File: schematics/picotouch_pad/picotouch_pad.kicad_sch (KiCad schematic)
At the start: 82 parts, among them SW1 1, SW10 1, SW11 1, SW12 1, SW13 1, SW14 1, SW15 1, SW16 1, SW17 1, SW18 1, SW19 1, SW2 1, SW20 1, SW21 1, SW22 1, SW23 1, SW3 1, SW4 1, SW5 1, SW6 1, SW7 1, SW8 1, SW9 1, U1 Pico

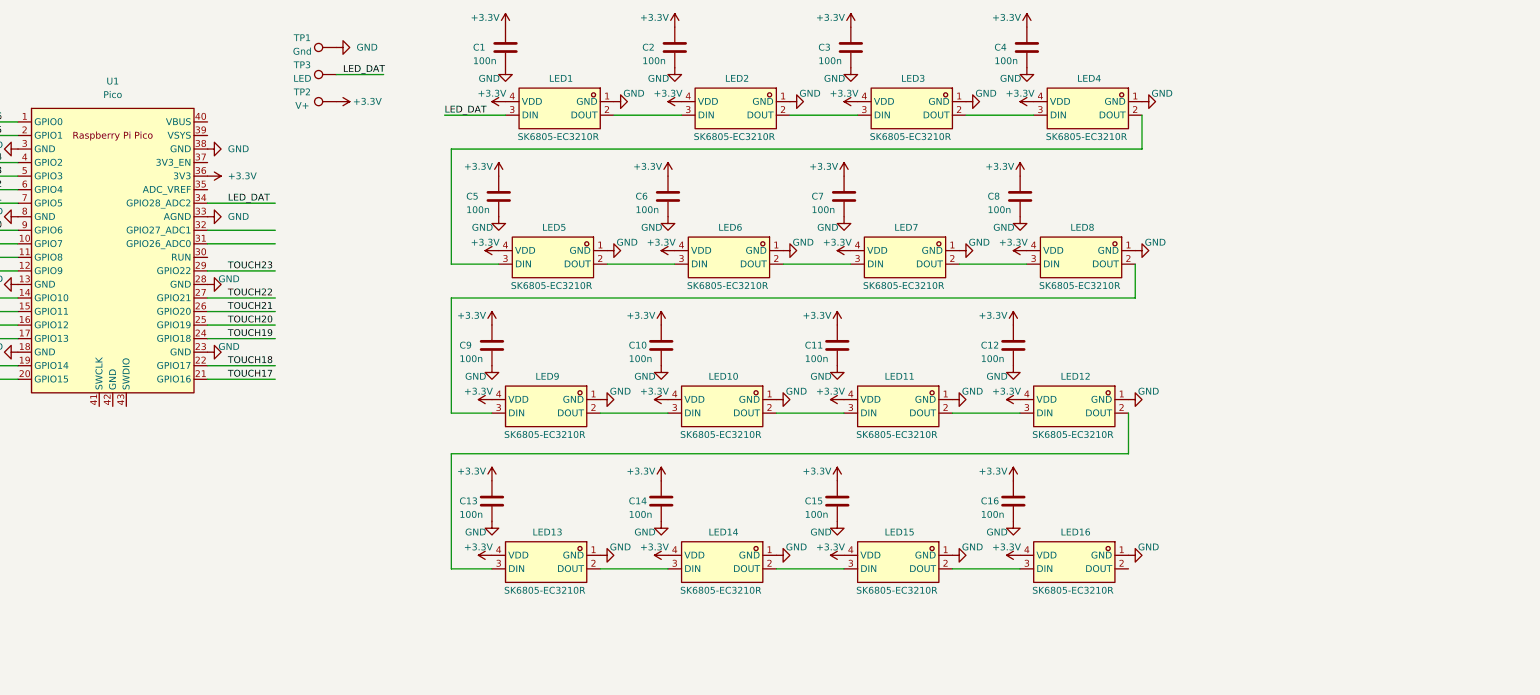
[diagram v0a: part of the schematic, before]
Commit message: new pcb with sk6812side
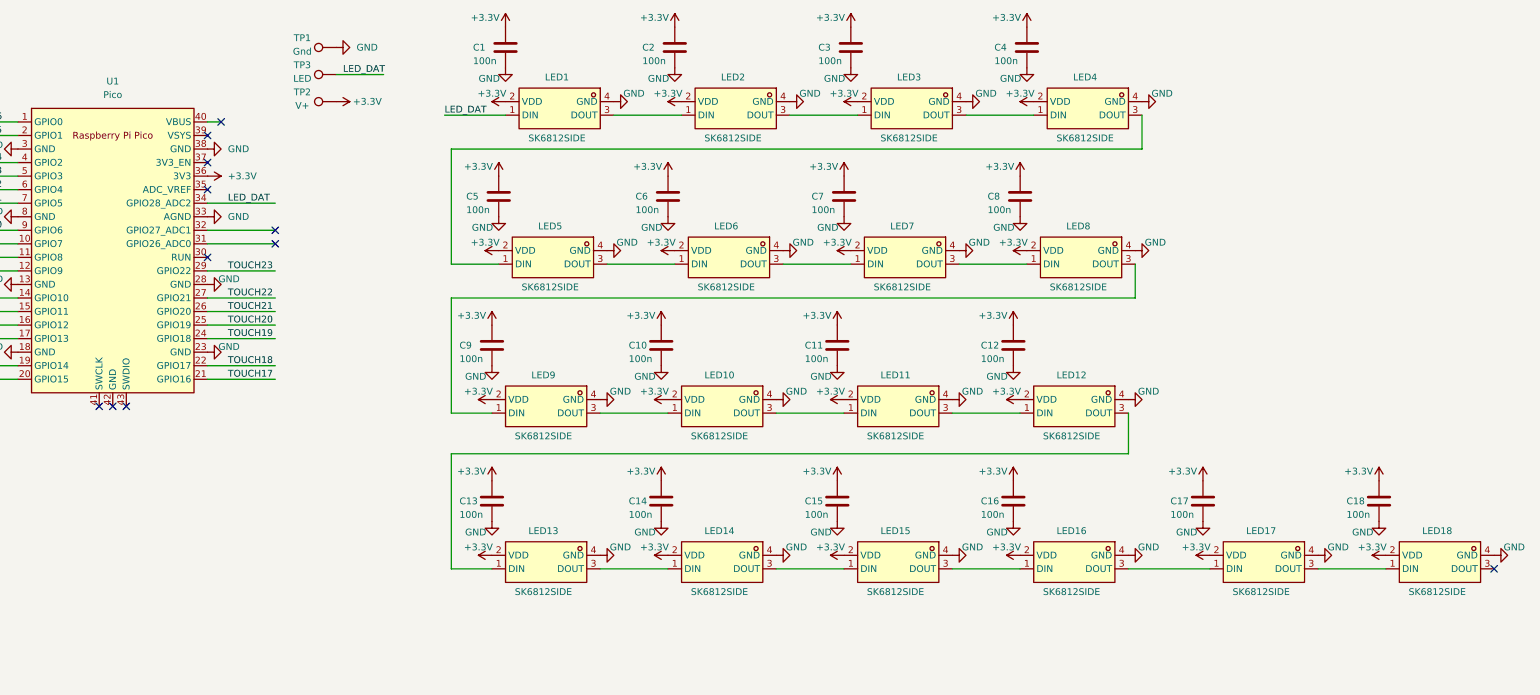
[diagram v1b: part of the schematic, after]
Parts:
- removed LED1, LED10, LED11, LED12, LED13, LED14, LED15, LED16, LED2, LED3, LED4, LED5, LED6, LED7, LED8, LED9: SK6805-EC3210R, todbot_stuff:LED-SMD_4P-L3.2-W1.5_SK6805-EC3210R-keepout, symbol todbot_stuff:SK6805-EC3210R
- added C17, C18: 100n, Capacitor_SMD:C_0603_1608Metric, symbol Device:C
- added LED1, LED10, LED11, LED12, LED13, LED14, LED15, LED16, LED17, LED18, LED2, LED3, LED4, LED5, LED6, LED7, LED8, LED9: SK6812SIDE, todbot_stuff:LED-SMD_4P-L4.0-W1.6-L-keepoutrev, symbol todbot_stuff:SK6812SIDE
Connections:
- net +3.3V: now also C17.1, C18.1, LED1.2 (VDD), LED10.2 (VDD), LED11.2 (VDD), LED12.2 (VDD), LED13.2 (VDD), LED14.2 (VDD), LED15.2 (VDD), LED16.2 (VDD), LED17.2 (VDD), LED18.2 (VDD), LED2.2 (VDD), LED3.2 (VDD), LED4.2 (VDD), LED5.2 (VDD), LED6.2 (VDD), LED7.2 (VDD), LED8.2 (VDD), LED9.2 (VDD)
- net GND: now also C17.2, C18.2, LED1.4 (GND), LED10.4 (GND), LED11.4 (GND), LED12.4 (GND), LED13.4 (GND), LED14.4 (GND), LED15.4 (GND), LED16.4 (GND), LED17.4 (GND), LED18.4 (GND), LED2.4 (GND), LED3.4 (GND), LED4.4 (GND), LED5.4 (GND), LED6.4 (GND), LED7.4 (GND), LED8.4 (GND), LED9.4 (GND)
- net LED_DAT: now also LED1.1 (DIN)
- new net: LED12.3 (DOUT), LED13.1 (DIN)
- new net: LED13.3 (DOUT), LED14.1 (DIN)
- new net: LED6.3 (DOUT), LED7.1 (DIN)
- new net: LED7.3 (DOUT), LED8.1 (DIN)
- new net: LED10.1 (DIN), LED9.3 (DOUT)
- new net: LED10.3 (DOUT), LED11.1 (DIN)
- new net: LED1.3 (DOUT), LED2.1 (DIN)
- new net: LED2.3 (DOUT), LED3.1 (DIN)
- new net: LED3.3 (DOUT), LED4.1 (DIN)
- new net: LED8.3 (DOUT), LED9.1 (DIN)
- new net: LED14.3 (DOUT), LED15.1 (DIN)
- new net: LED15.3 (DOUT), LED16.1 (DIN)
- new net: LED16.3 (DOUT), LED17.1 (DIN)
- new net: LED5.3 (DOUT), LED6.1 (DIN)
- new net: LED4.3 (DOUT), LED5.1 (DIN)
- new net: LED17.3 (DOUT), LED18.1 (DIN)
- new net: LED11.3 (DOUT), LED12.1 (DIN)
- no-connect marks 0 -> 11

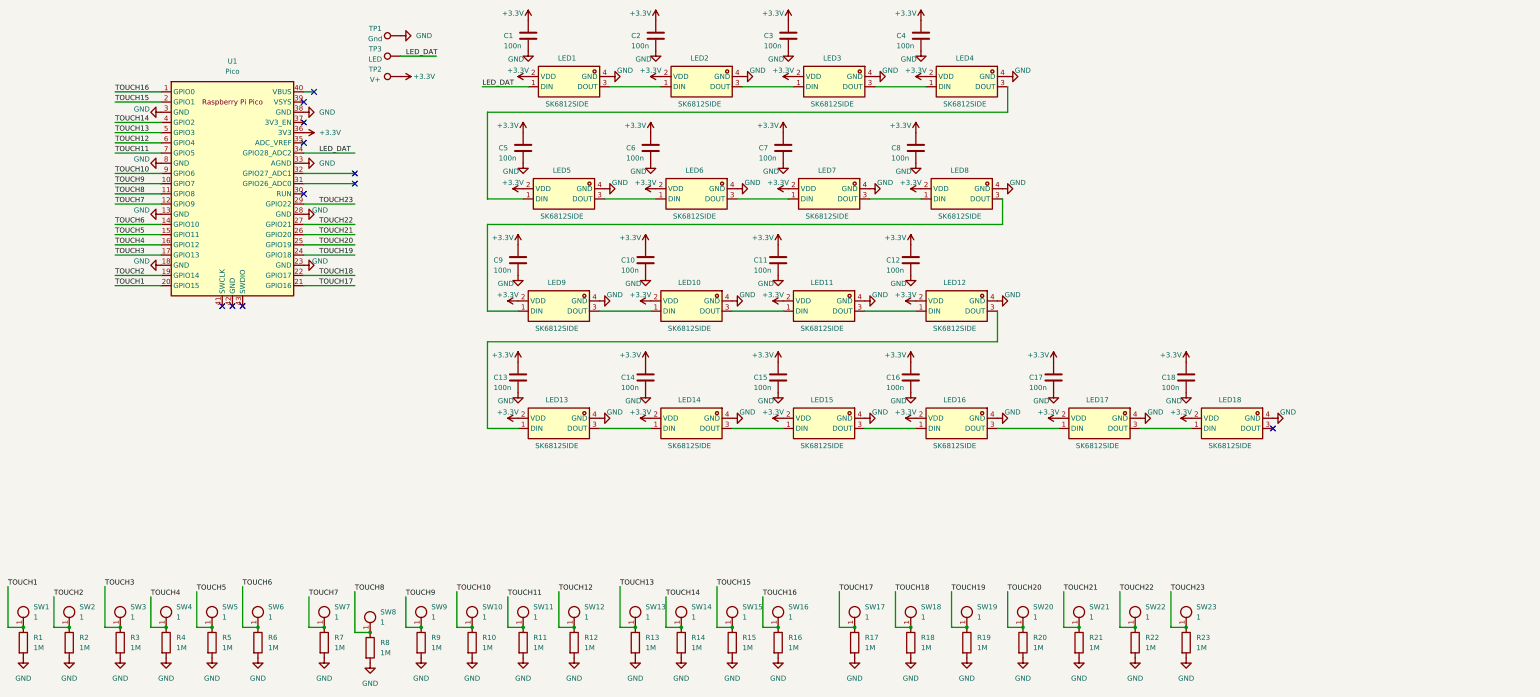
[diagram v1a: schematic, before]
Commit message: add battery circuit
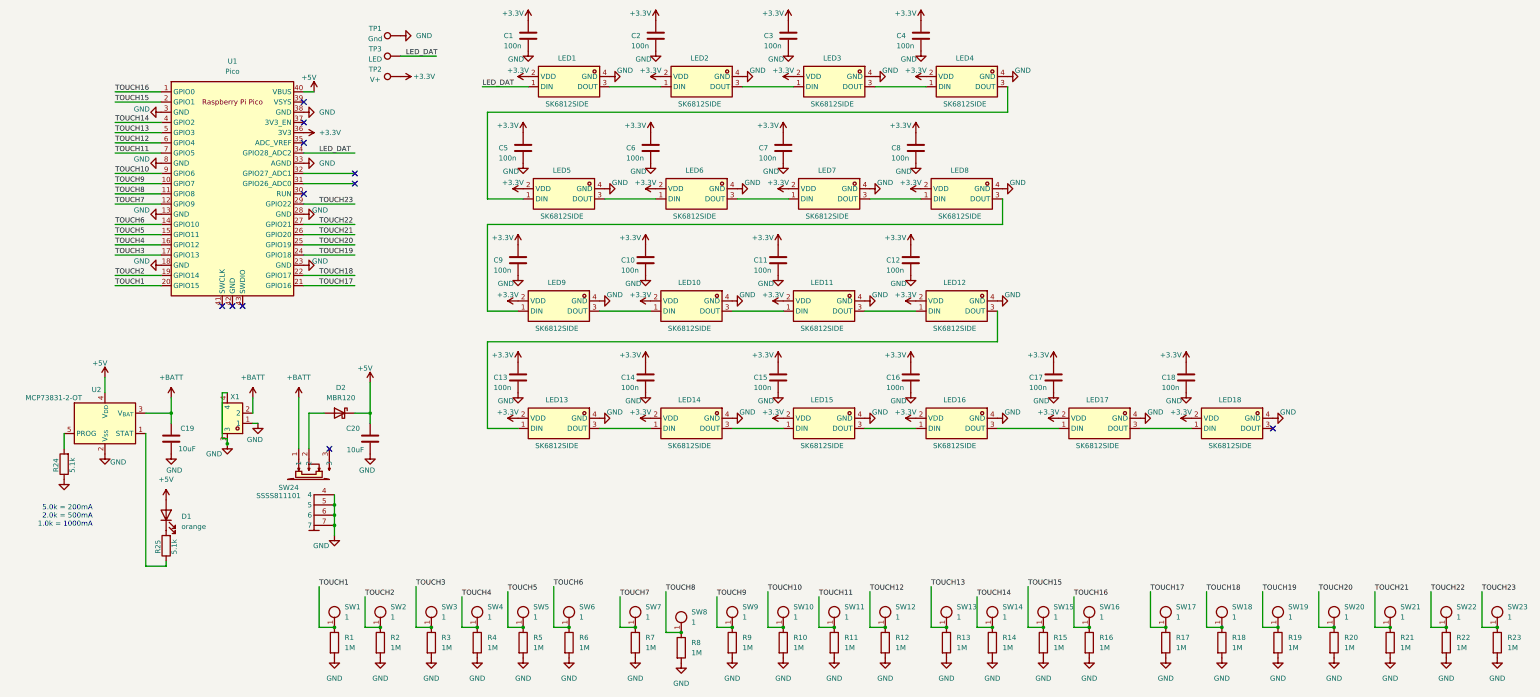
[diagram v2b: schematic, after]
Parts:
- added C19, C20: 10uF, Capacitor_SMD:C_0603_1608Metric, symbol Device:C
- added D1: orange, LED_SMD:LED_0603_1608Metric, symbol Device:LED
- added D2: MBR120, Diode_SMD:D_SOD-123F, symbol Device:D_Schottky
- added R24, R25: 5.1k, Resistor_SMD:R_0603_1608Metric, symbol Device:R
- added SW24: SSSS811101, easyeda2kicad:SW-SMD_SSSS811101, symbol easyeda2kicad:SSSS811101
- added U2: MCP73831-2-OT, Package_TO_SOT_SMD:SOT-23-5, symbol Battery_Management:MCP73831-2-OT
- added X1: AFC20-S02ACA-00, easyeda2kicad:CONN-SMD_AFC20-S02ACA-00, symbol easyeda2kicad:AFC20-S02ACA-00
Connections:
- net GND: now also C19.2, C20.2, R24.1, SW24.4, SW24.5, SW24.6, SW24.7, U2.2 (V_{SS}), X1.1, X1.3, X1.4
- net +5V: now reaches U1.40 (VBUS)
- net +5V: now also C20.1, D1.2 (A), D2.1 (K), U2.4 (V_{DD})
- new net: R25.1, U2.1 (STAT)
- new net: R24.2, U2.5 (PROG)
- new net: D1.1 (K), R25.2
- new net: D2.2 (A), SW24.2
- new net +BATT: C19.1, SW24.1, U2.3 (V_{BAT}), X1.2
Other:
- note added: "5.0k = 200mA 2.0k = 500mA 1.0k = 1000mA"
- moved on the sheet: R1, R10, R11, R12, R13, R14, R15, R16, R17, R18, R19, R2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

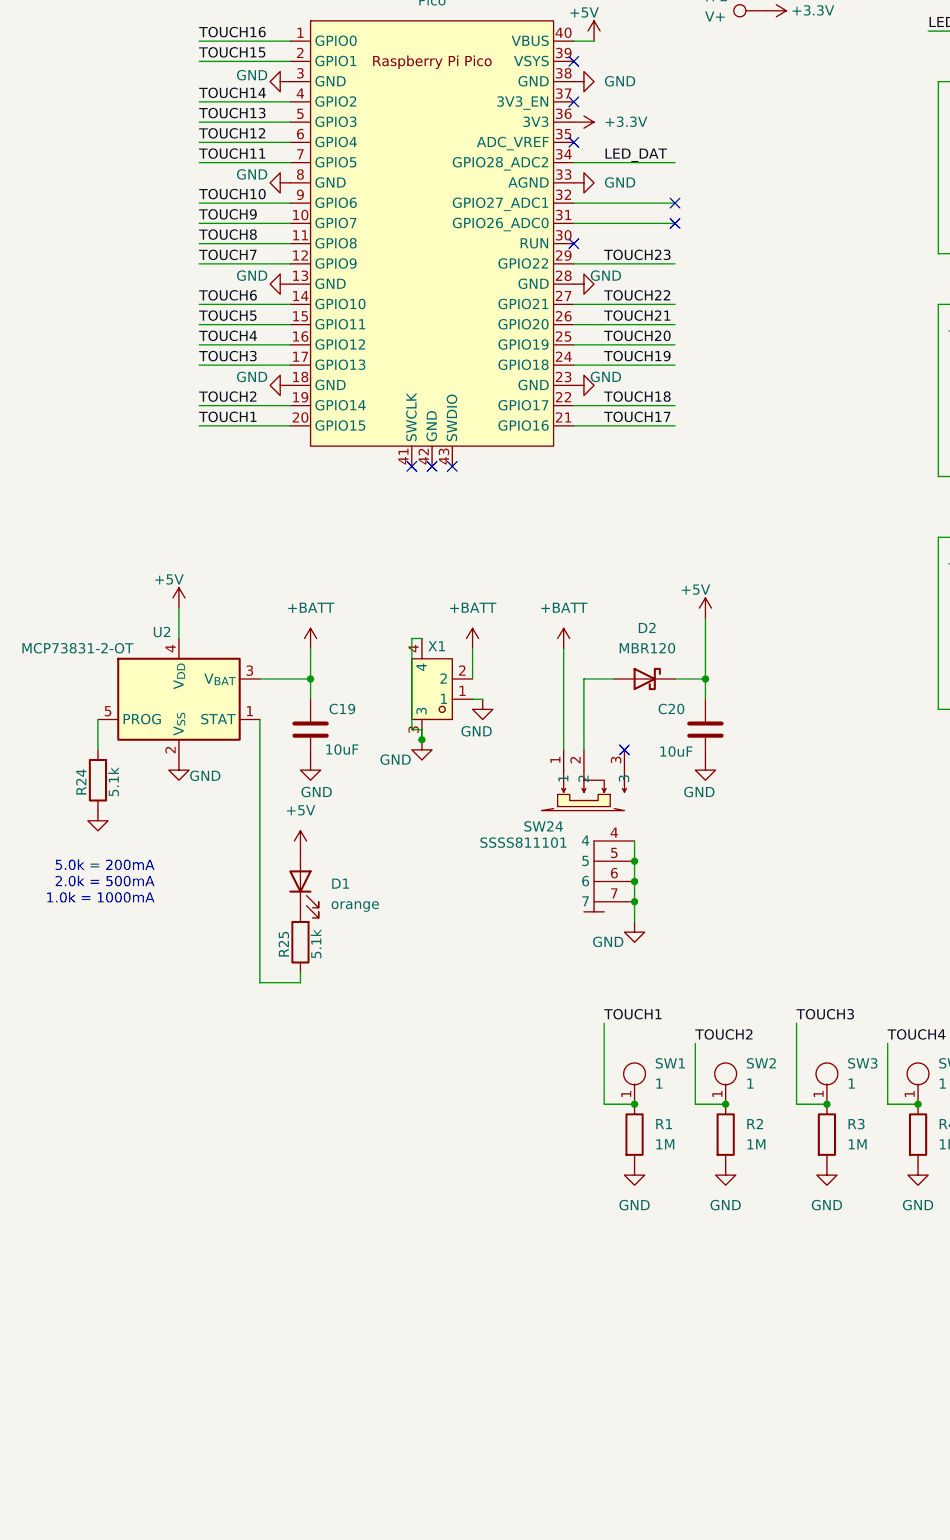
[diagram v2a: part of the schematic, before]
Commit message: add midi out
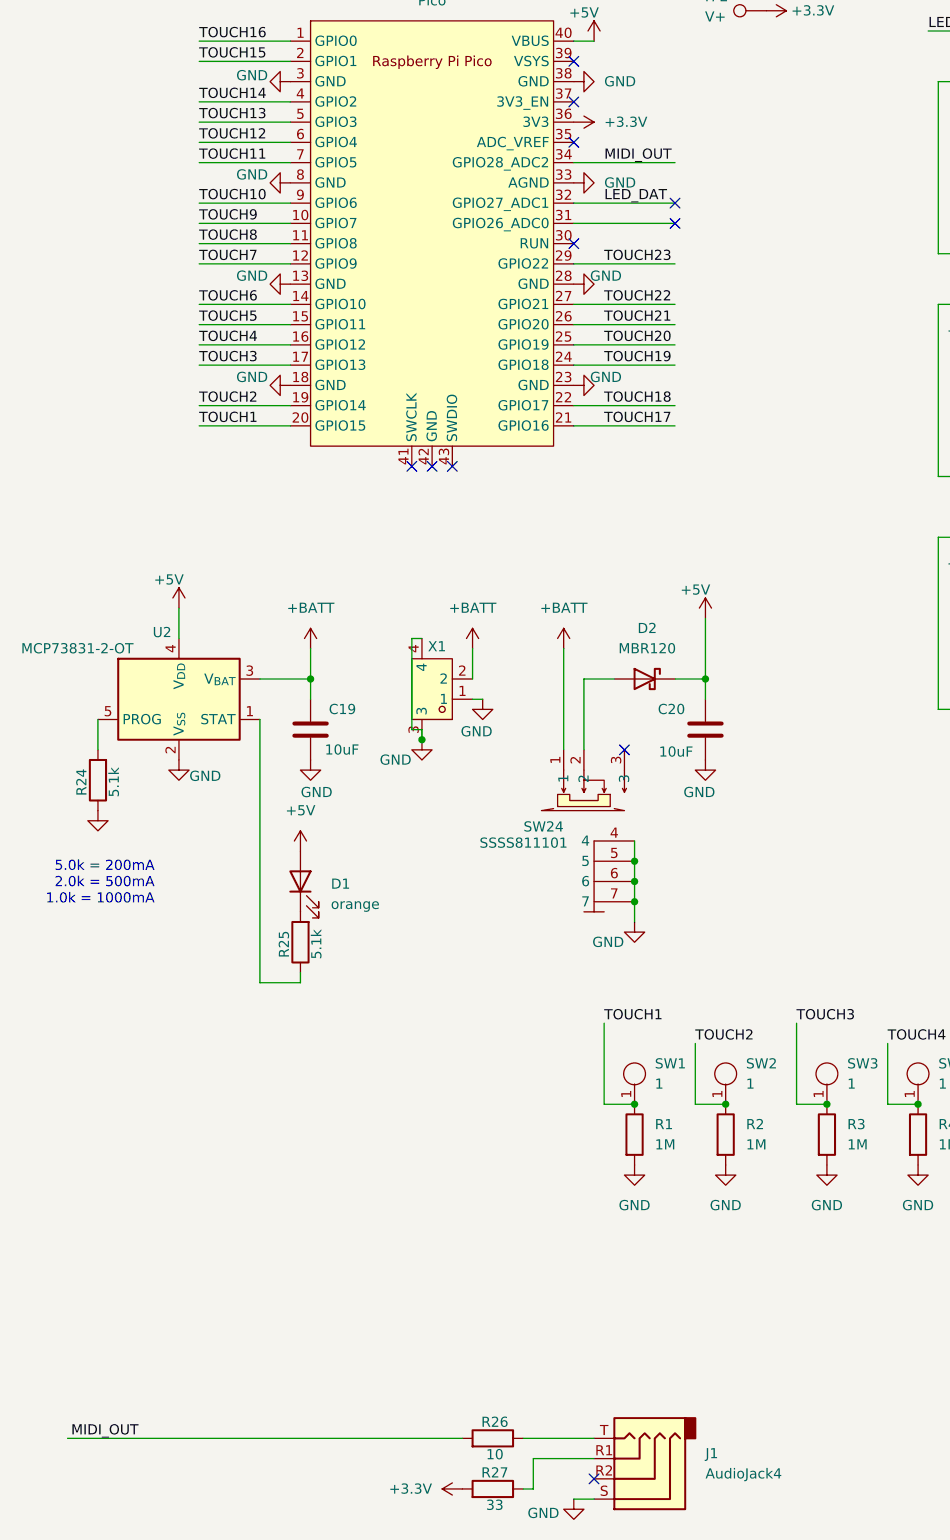
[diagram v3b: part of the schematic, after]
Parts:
- added J1: AudioJack4, todbot_stuff:Jack_3.5mm_PJ320D_Horizontal, symbol Connector_Audio:AudioJack4
- added R26: 10, Resistor_SMD:R_0603_1608Metric, symbol Device:R
- added R27: 33, Resistor_SMD:R_0603_1608Metric, symbol Device:R
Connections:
- net +3.3V: now also R27.2
- net GND: now also J1.S
- net LED_DAT: now also U1.32 (GPIO27_ADC1); no longer U1.34 (GPIO28_ADC2)
- new net: J1.R1, R27.1
- new net: J1.T, R26.1
- new net MIDI_OUT: R26.2, U1.34 (GPIO28_ADC2)
- no-connect marks 11 -> 12

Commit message: cleanup
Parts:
- renumbered SW1 to PAD1, SW10 to PAD10, SW11 to PAD11, SW12 to PAD12, SW13 to PAD13, SW14 to PAD14, SW15 to PAD15, SW16 to PAD16, SW17 to PAD17, SW18 to PAD18, SW19 to PAD19, SW2 to PAD2, SW20 to PAD20, SW21 to PAD21, SW22 to PAD22, SW23 to PAD23, SW3 to PAD3, SW4 to PAD4, SW5 to PAD5, SW6 to PAD6, SW7 to PAD7, SW8 to PAD8, SW9 to PAD9, SW24 to SW1
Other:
- note added: "PROG R 5.0k = 200mA 2.0k = 500mA 1.0k = 1000mA"
- note added: "adapted from Adafruit Lipoly BFF"
- note added: "charge"
- note removed: "5.0k = 200mA 2.0k = 500mA 1.0k = 1000mA"
- moved on the sheet: C1, C10, C11, C12, C13, C14, C15, C16, C17, C18, C19, C2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
